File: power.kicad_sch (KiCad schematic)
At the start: 56 parts, among them J1 PWR + CAN harness, Q1 100V 4.3mOhm N-ch, U1 LM74700-Q1, U2 LM5164-Q1 (5V), U3 LM5164-Q1 (3V3)

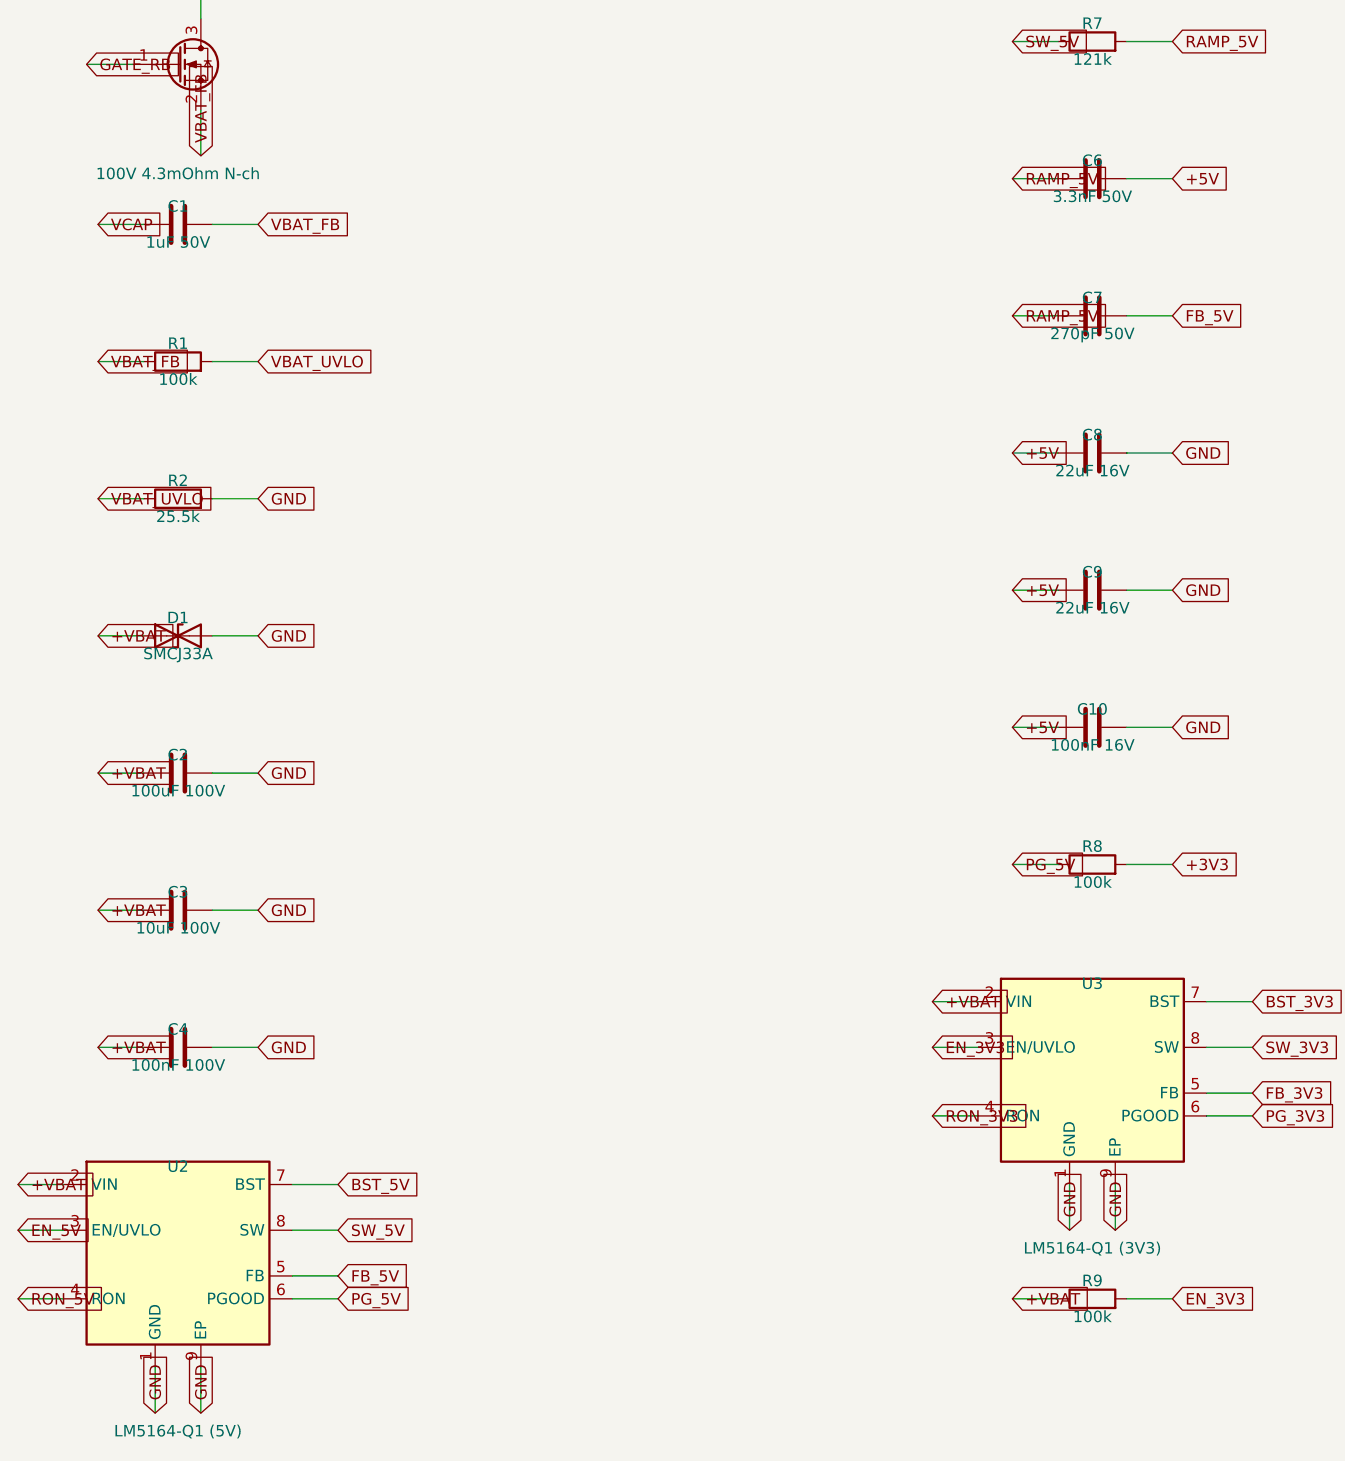
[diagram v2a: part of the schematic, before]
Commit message: Source the BOM for JLCPCB assembly; fix a nonexistent FET part number
Availability check against LCSC / DigiKey / Mouser (2026-08), with the
board now targeted at JLCPCB pick-and-place:

- Q1 was specified as PSMN4R3-100BSE, a part number that does not exist
  (Nexperia's nearest real part is the D2PAK PSMN4R8-100BSE, which would
  not fit the TO-252 footprint anyway). Replaced with Infineon
  IPD068N10N3G (LCSC C88066): DPAK, 100V, 6.8mOhm, in stock.
- LM5164QDDARQ1 is backordered at DigiKey and nearly dry at Mouser;
  switched to the non-automotive LM5164DDAR (LCSC C477928, DigiKey 3.4k
  in stock). Same silicon, minus AEC-Q100.
- ADS1115QDGSRQ1 requires a manufacturer quote at DigiKey; switched to
  ADS1115IDGSR (LCSC C37593, in stock).

README gains a sourcing table with LCSC part numbers for the critical
semiconductors and a list of what still gets picked from the live JLC
catalog at layout time (buck inductors, bulk electrolytic, 0.1%
resistors).

Validated with kicad-cli 9.0: 104 nets / 162 instances match, ERC clean.

Co-Authored-By: Claude Fable 5 <noreply@anthropic.com>
Claude-Session: https://claude.ai/code/session_01DhNbL25h25p8VFCjRfJik9
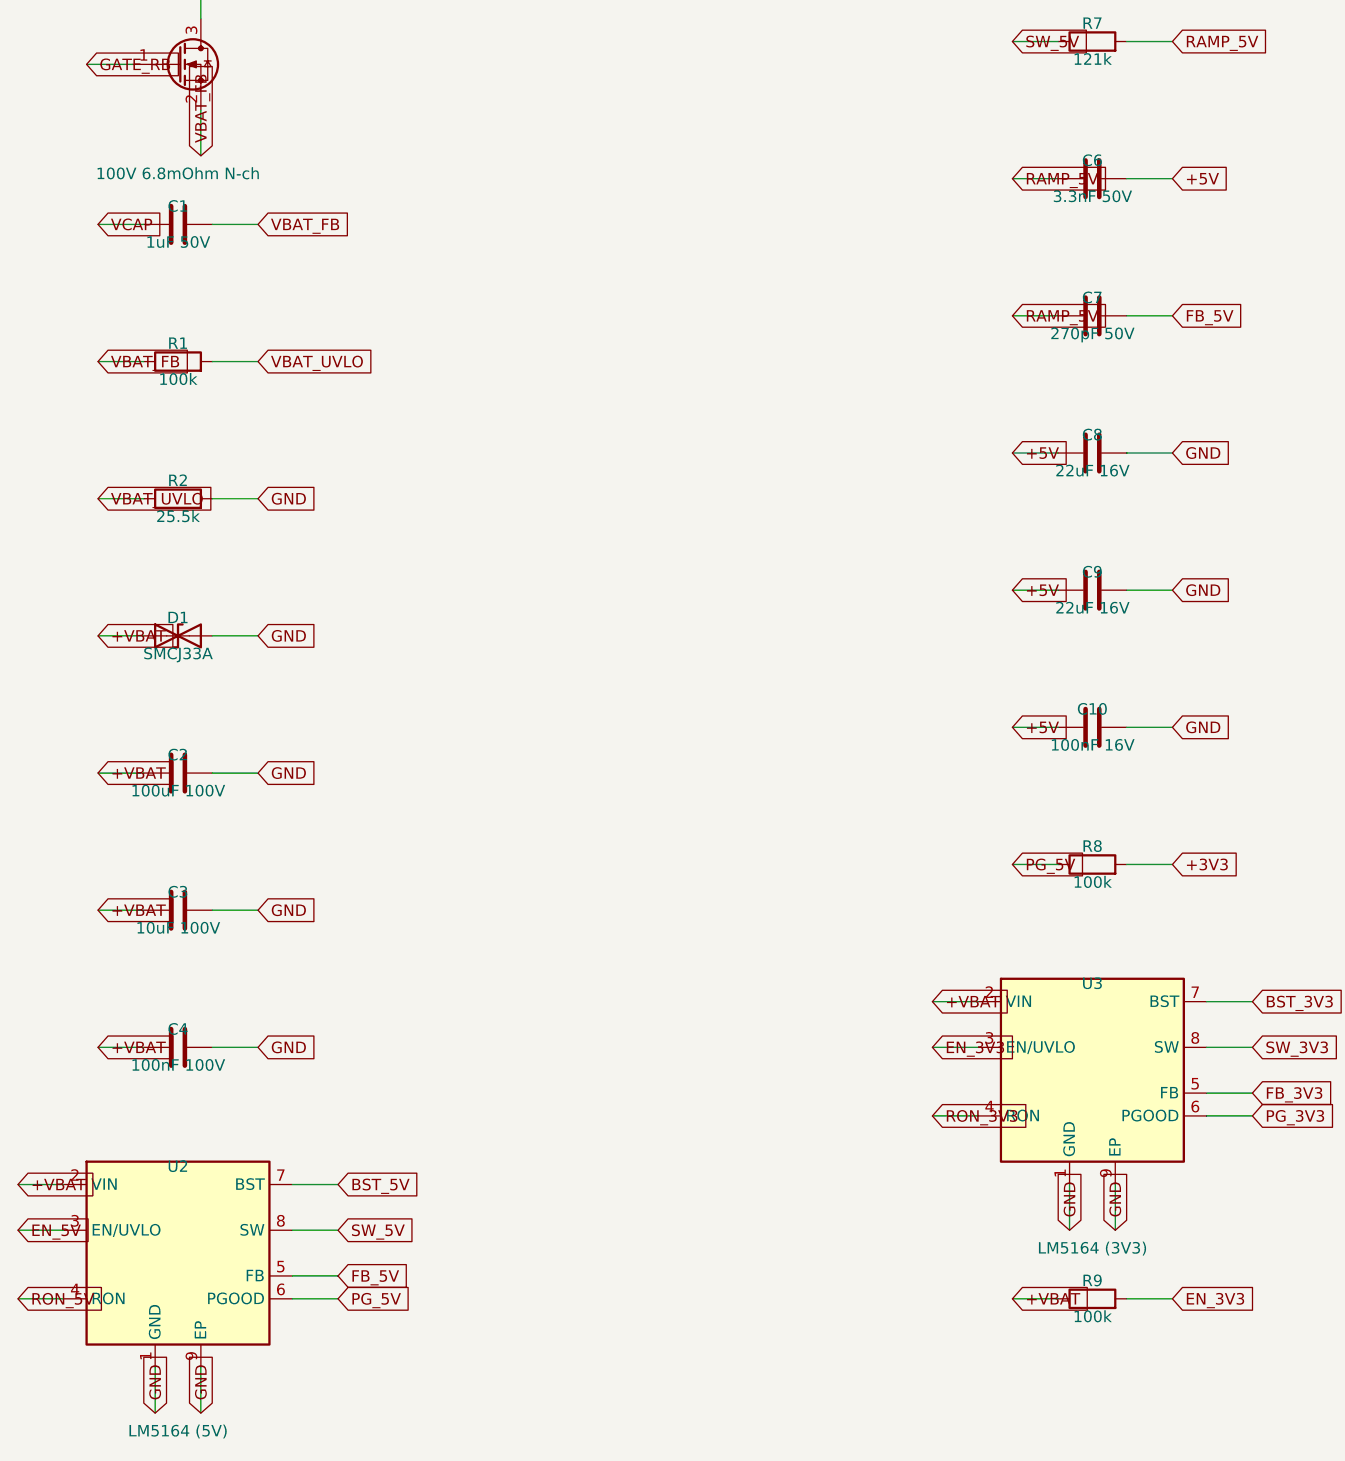
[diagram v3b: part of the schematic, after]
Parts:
- Q1: value 100V 4.3mOhm N-ch -> 100V 6.8mOhm N-ch; MPN Nexperia PSMN4R3-100BSE -> Infineon IPD068N10N3G; Note Source to battery, drain to load: body diode blocks reverse polarity -> Source to battery, drain to load: body diode blocks reverse polarity. LCSC C88066; the previously specified PSMN4R3-100BSE does not exist
- U2: value LM5164-Q1 (5V) -> LM5164 (5V); MPN LM5164QDDARQ1 -> LM5164DDAR; Note 100V synchronous buck, ultra-low Iq -> 100V synchronous buck, ultra-low Iq. Non-automotive variant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
- U3: value LM5164-Q1 (3V3) -> LM5164 (3V3); MPN LM5164QDDARQ1 -> LM5164DDAR
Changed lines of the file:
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@@
       (effects (font (size 1.27 1.27)) )
     )
-    (property "Value" "100V 4.3mOhm N-ch" (at 59.69 123.92 0)
+    (property "Value" "100V 6.8mOhm N-ch" (at 59.69 123.92 0)
       (effects (font (size 1.27 1.27)) )
     )
@@
       (effects (font (size 1.27 1.27)) hide)
     )
-    (property "MPN" "Nexperia PSMN4R3-100BSE" (at 59.69 123.92 0)
-      (effects (font (size 1.27 1.27)) hide)
-    )
-    (property "Note" "Source to battery, drain to load: body diode blocks reverse polarity" (at 59.69 123.92 0)
+    (property "MPN" "Infineon IPD068N10N3G" (at 59.69 123.92 0)
+      (effects (font (size 1.27 1.27)) hide)
+    )
+    (property "Note" "Source to battery, drain to load: body diode blocks reverse polarity. LCSC C88066; the previously specified PSMN4R3-100BSE does not exist" (at 59.69 123.92 0)
       (effects (font (size 1.27 1.27)) hide)
     )
@@
       (effects (font (size 1.27 1.27)) )
     )
-    (property "Value" "LM5164-Q1 (5V)" (at 59.69 263.62 0)
+    (property "Value" "LM5164 (5V)" (at 59.69 263.62 0)
       (effects (font (size 1.27 1.27)) )
     )
@@
       (effects (font (size 1.27 1.27)) hide)
     )
-    (property "MPN" "LM5164QDDARQ1" (at 59.69 263.62 0)
-      (effects (font (size 1.27 1.27)) hide)
-    )
-    (property "Note" "100V synchronous buck, ultra-low Iq" (at 59.69 263.62 0)
+    (property "MPN" "LM5164DDAR" (at 59.69 263.62 0)
+      (effects (font (size 1.27 1.27)) hide)
+    )
+    (property "Note" "100V synchronous buck, ultra-low Iq. Non-automotive variant: LCSC C477928 and DigiKey stock it; the Q1 is scarce" (at 59.69 263.62 0)
       (effects (font (size 1.27 1.27)) hide)
     )
@@
       (effects (font (size 1.27 1.27)) )
     )
-    (property "Value" "LM5164-Q1 (3V3)" (at 161.29 243.3 0)
+    (property "Value" "LM5164 (3V3)" (at 161.29 243.3 0)
       (effects (font (size 1.27 1.27)) )
     )
@@
       (effects (font (size 1.27 1.27)) hide)
     )
-    (property "MPN" "LM5164QDDARQ1" (at 161.29 243.3 0)
-      (effects (font (size 1.27 1.27)) hide)
-    )
+    (property "MPN" "LM5164DDAR" (at 161.29 243.3 0)
+      (effects (font (size 1.27 1.27)) hide)
+    )

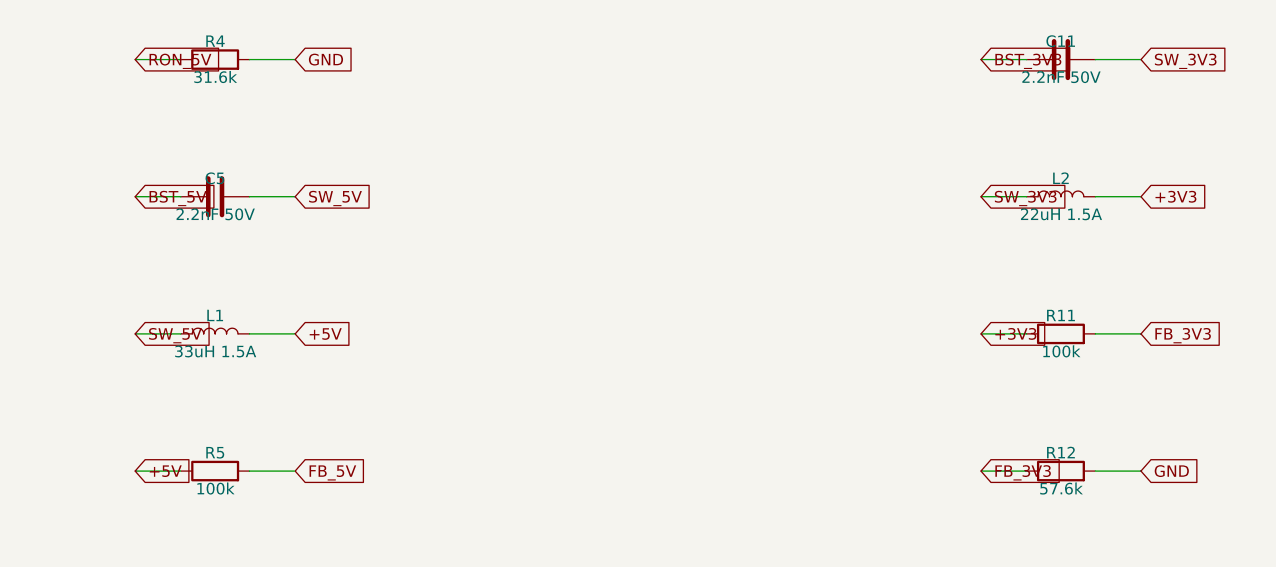
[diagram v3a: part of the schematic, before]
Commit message: Generate the 4-layer board: placed, DRC-clean, ready to route
gen/generate_pcb.py (runs under KiCad 9's bundled Python) builds
esp32s3-can-sd-logger.kicad_pcb from the same part/net tables as the
schematic generator: real library footprints, every pad netted, and
zone-based placement -- harness connectors on the left edge, analog
channel columns and the ESP32 with its antenna overhanging the top edge
(module keepout falls off-board), USB-C/microSD/buttons on the right,
battery front end and both bucks in the bottom band, GND and +3V3
inner-plane zones, JLC-compatible 0.2mm minimum drill.

84 x 72 mm. kicad-cli pcb drc: zero violations; the 335 unconnected
items are the unrouted ratsnest.

Also adds the project footprint library (TDK ACT45B CAN choke built from
the datasheet land pattern) and a placement render under plots/.

Co-Authored-By: Claude Fable 5 <noreply@anthropic.com>
Claude-Session: https://claude.ai/code/session_01DhNbL25h25p8VFCjRfJik9
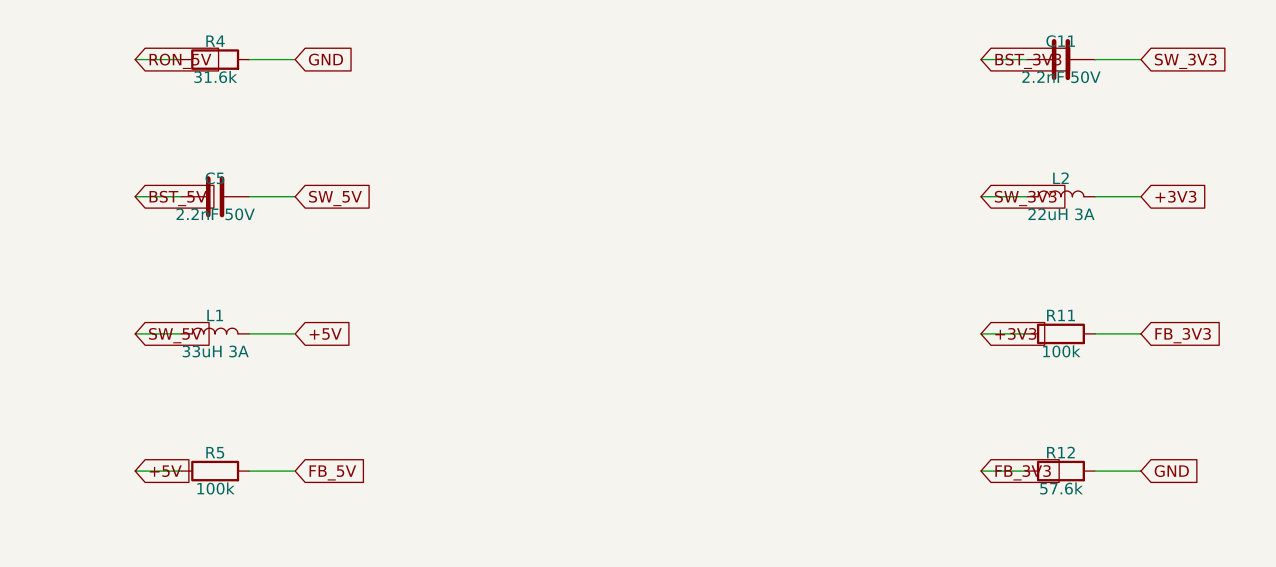
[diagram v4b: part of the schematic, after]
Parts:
- C2: Note Bulk hold-up -> Bulk hold-up; any 100uF >=80V SMD electrolytic on a 10x10.5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
- J1: MPN JST B4B-PH-K -> JST B4B-PH-K-S(LF)(SN)
- L1: value 33uH 1.5A -> 33uH 3A; footprint Inductor_SMD:L_7.3x7.3_H4.5 -> Inductor_SMD:L_Sunlord_SWPA8040S; MPN Coilcraft XAL7030-333 -> Sunlord ASWPA8050S330MT; Note Shielded, Isat > 2A -> Shielded molded, Isat 3A vs the 1.75A max peak limit
- L2: value 22uH 1.5A -> 22uH 3A; footprint Inductor_SMD:L_7.3x7.3_H4.5 -> Inductor_SMD:L_Sunlord_SWPA8040S; MPN Coilcraft XAL7030-223 -> Sunlord ASWPA8050S220MT; Note (none) -> Same automotive series as L1
- Q1: Note Source to battery, drain to load: body diode blocks reverse polarity. LCSC C88066; the previously specified PSMN4R3-100BSE does not exist -> Source to battery, drain to load: body diode blocks reverse polarity. The previously specified PSMN4R3-100BSE does not exist
- U2: Note 100V synchronous buck, ultra-low Iq. Non-automotive variant: LCSC C477928 and DigiKey stock it; the Q1 is scarce -> 100V synchronous buck, ultra-low Iq. Non-automotive variant; the Q1 is scarce
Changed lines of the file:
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@@
       (effects (font (size 1.27 1.27)) hide)
     )
-    (property "MPN" "JST B4B-PH-K" (at 59.69 27.4 0)
+    (property "MPN" "JST B4B-PH-K-S(LF)(SN)" (at 59.69 27.4 0)
       (effects (font (size 1.27 1.27)) hide)
     )
@@
       (effects (font (size 1.27 1.27)) hide)
     )
-    (property "Note" "Source to battery, drain to load: body diode blocks reverse polarity. LCSC C88066; the previously specified PSMN4R3-100BSE does not exist" (at 59.69 123.92 0)
+    (property "Note" "Source to battery, drain to load: body diode blocks reverse polarity. The previously specified PSMN4R3-100BSE does not exist" (at 59.69 123.92 0)
       (effects (font (size 1.27 1.27)) hide)
     )
@@
       (effects (font (size 1.27 1.27)) hide)
     )
-    (property "Note" "Bulk hold-up" (at 59.69 192.5 270)
+    (property "Note" "Bulk hold-up; any 100uF >=80V SMD electrolytic on a 10x10.5 land works -- match in the JLC catalog at order" (at 59.69 192.5 270)
       (effects (font (size 1.27 1.27)) hide)
     )
@@
       (effects (font (size 1.27 1.27)) hide)
     )
-    (property "Note" "100V synchronous buck, ultra-low Iq. Non-automotive variant: LCSC C477928 and DigiKey stock it; the Q1 is scarce" (at 59.69 263.62 0)
+    (property "Note" "100V synchronous buck, ultra-low Iq. Non-automotive variant; the Q1 is scarce" (at 59.69 263.62 0)
       (effects (font (size 1.27 1.27)) hide)
     )
@@
       (effects (font (size 1.27 1.27)) )
     )
-    (property "Value" "33uH 1.5A" (at 161.29 65.5 270)
-      (effects (font (size 1.27 1.27)) )
-    )
-    (property "Footprint" "Inductor_SMD:L_7.3x7.3_H4.5" (at 161.29 65.5 270)
+    (property "Value" "33uH 3A" (at 161.29 65.5 270)
+      (effects (font (size 1.27 1.27)) )
+    )
+    (property "Footprint" "Inductor_SMD:L_Sunlord_SWPA8040S" (at 161.29 65.5 270)
       (effects (font (size 1.27 1.27)) hide)
     )
@@
       (effects (font (size 1.27 1.27)) hide)
     )
-    (property "MPN" "Coilcraft XAL7030-333" (at 161.29 65.5 270)
-      (effects (font (size 1.27 1.27)) hide)
-    )
-    (property "Note" "Shielded, Isat > 2A" (at 161.29 65.5 270)
+    (property "MPN" "Sunlord ASWPA8050S330MT" (at 161.29 65.5 270)
+      (effects (font (size 1.27 1.27)) hide)
+    )
+    (property "Note" "Shielded molded, Isat 3A vs the 1.75A max peak limit" (at 161.29 65.5 270)
       (effects (font (size 1.27 1.27)) hide)
     )
@@
       (effects (font (size 1.27 1.27)) )
     )
-    (property "Value" "22uH 1.5A" (at 255.27 50.26 270)
-      (effects (font (size 1.27 1.27)) )
-    )
-    (property "Footprint" "Inductor_SMD:L_7.3x7.3_H4.5" (at 255.27 50.26 270)
+    (property "Value" "22uH 3A" (at 255.27 50.26 270)
+      (effects (font (size 1.27 1.27)) )
+    )
+    (property "Footprint" "Inductor_SMD:L_Sunlord_SWPA8040S" (at 255.27 50.26 270)
       (effects (font (size 1.27 1.27)) hide)
     )
@@
       (effects (font (size 1.27 1.27)) hide)
     )
-    (property "MPN" "Coilcraft XAL7030-223" (at 255.27 50.26 270)
-      (effects (font (size 1.27 1.27)) hide)
-    )
+    (property "MPN" "Sunlord ASWPA8050S220MT" (at 255.27 50.26 270)
+      (effects (font (size 1.27 1.27)) hide)
+    )
+    (property "Note" "Same automotive series as L1" (at 255.27 50.26 270)
+      (effects (font (size 1.27 1.27)) hide)
+    )
